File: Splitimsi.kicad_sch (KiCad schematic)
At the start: 44 parts, among them SW1 MX_RGB, SW10 MX_RGB, SW11 MX_RGB, SW12 RotaryEncoder_Switch, SW13 MX_RGB, SW14 MX_RGB, SW15 MX_RGB, SW16 MX_RGB, SW17 MX_RGB, SW18 MX_RGB, SW19 MX_RGB, SW2 MX_RGB, SW20 MX_RGB, SW21 MX_RGB, SW22 MX_RGB, SW23 MX_RGB, SW24 MX_RGB, SW25 MX_RGB, SW26 MX_RGB, SW27 MX_RGB, SW28 MX_RGB, SW29 MX_RGB, SW3 MX_RGB, SW30 MX_RGB, SW4 MX_RGB, SW5 MX_RGB, SW6 RotaryEncoder_Switch, SW7 MX_RGB, SW8 MX_RGB, SW9 MX_RGB, U1 ProMicro, U2 TRRS

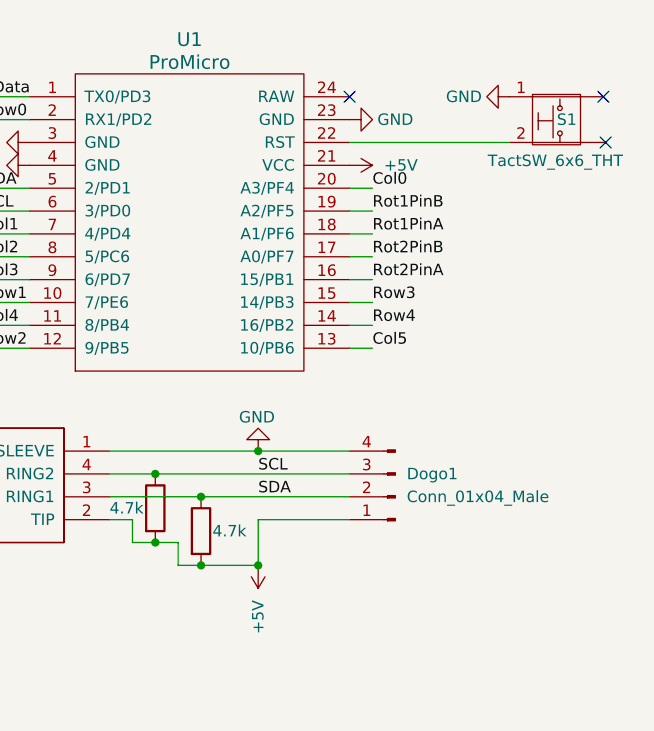
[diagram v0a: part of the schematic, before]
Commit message: reset schematic changed
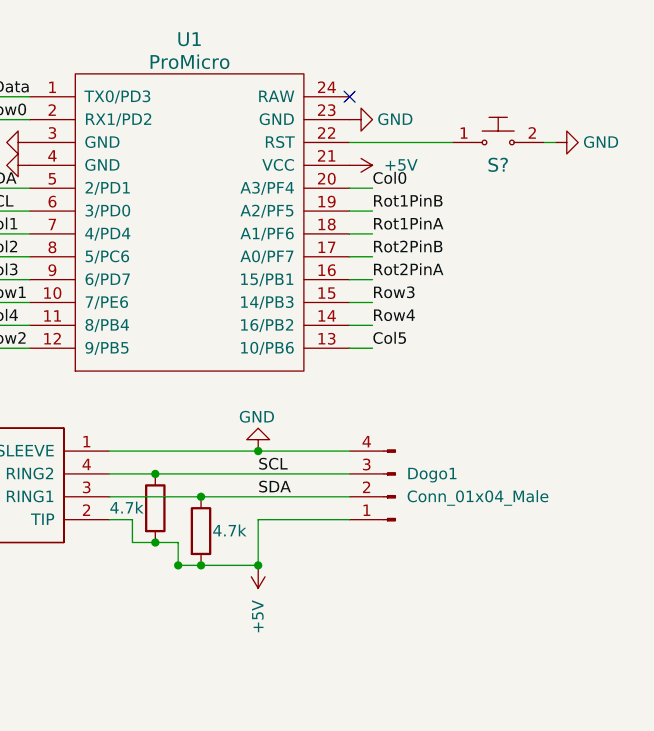
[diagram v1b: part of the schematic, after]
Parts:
- removed S1: TactSW_6x6_THT, Button_Switch_SMD:SW_SPST_B3U-1000P, symbol KeyboardCustomSym:TactSW_6x6_THT
- added S?: (no value), symbol dk_Tactile-Switches:B3U-1000P
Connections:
- net GND: now also S?.2
- net at U1.22 (RST): now also S?.1
- no-connect marks 3 -> 1
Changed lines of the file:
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@@
   (junction (at 63.5 101.6) (diameter 0) (color 0 0 0 0)
   )
+  (junction (at 170.18 73.66) (diameter 0) (color 0 0 0 0)
+  )
   (junction (at 73.66 71.12) (diameter 0) (color 0 0 0 0)
   )
@@
   )
   (no_connect (at 189.23 21.59))
-  (no_connect (at 217.424 21.59))
-  (no_connect (at 217.678 26.67))
+  (wire (pts (xy 210.82 26.67) (xy 212.09 26.67))
+    (stroke (width 0) (type default) (color 0 0 0 0))
+  )
   (wire (pts (xy 71.12 96.52) (xy 71.12 99.06))
     (stroke (width 0) (type default) (color 0 0 0 0))
@@
     (stroke (width 0) (type default) (color 0 0 0 0))
   )
-  (wire (pts (xy 189.23 26.67) (xy 207.01 26.67))
+  (wire (pts (xy 189.23 26.67) (xy 200.66 26.67))
     (stroke (width 0) (type default) (color 0 0 0 0))
   )
@@
   )
   (wire (pts (xy 97.79 128.27) (xy 104.14 128.27))
+    (stroke (width 0) (type default) (color 0 0 0 0))
+  )
+  (wire (pts (xy 170.18 73.7663) (xy 170.18 73.66))
     (stroke (width 0) (type default) (color 0 0 0 0))
   )
@@
     (pin "1")
   )
-  (symbol (lib_id "power:GND") (at 207.01 21.59 270) (unit 1)
-    (in_bom yes) (on_board yes)
-    (property "Reference" "#PWR01" (id 0) (at 200.66 21.59 0)
-      (effects (font (size 1.27 1.27)) hide)
-    )
-    (property "Value" "GND" (id 1) (at 201.93 21.59 90))
-    (property "Footprint" "" (id 2) (at 207.01 21.59 0)
-      (effects (font (size 1.27 1.27)) hide)
-    )
-    (property "Datasheet" "" (id 3) (at 207.01 21.59 0)
+  (symbol (lib_id "power:GND") (at 212.09 26.67 90) (unit 1)
+    (in_bom yes) (on_board yes)
+    (property "Reference" "#PWR01" (id 0) (at 218.44 26.67 0)
+      (effects (font (size 1.27 1.27)) hide)
+    )
+    (property "Value" "GND" (id 1) (at 217.17 26.67 90))
+    (property "Footprint" "" (id 2) (at 212.09 26.67 0)
+      (effects (font (size 1.27 1.27)) hide)
+    )
+    (property "Datasheet" "" (id 3) (at 212.09 26.67 0)
       (effects (font (size 1.27 1.27)) hide)
     )
@@
     (pin "8")
   )
+  (symbol (lib_id "dk_Tactile-Switches:B3U-1000P") (at 205.74 26.67 0) (unit 1)
+    (in_bom yes) (on_board yes)
+    (property "Reference" "S?" (id 0) (at 205.74 29.21 0)
+      (effects (font (size 1.524 1.524)))
+    )
+    (property "Value" "" (id 1) (at 205.74 21.59 0)
+      (effects (font (size 1.524 1.524)))
+    )
+    (property "Footprint" "" (id 2) (at 210.82 21.59 0)
+      (effects (font (size 1.524 1.524)) (justify left) hide)
+    )
+    (property "Datasheet" "https://omronfs.omron.com/en_US/ecb/products/pdf/en-b3u.pdf" (id 3) (at 210.82 19.05 0)
+      (effects (font (size 1.524 1.524)) (justify left) hide)
+    )
+    (property "Digi-Key_PN" "SW1020CT-ND" (id 4) (at 210.82 16.51 0)
+      (effects (font (size 1.524 1.524)) (justify left) hide)
+    )
+    (property "MPN" "B3U-1000P" (id 5) (at 210.82 13.97 0)
+      (effects (font (size 1.524 1.524)) (justify left) hide)
+    )
+    (property "Category" "Switches" (id 6) (at 210.82 11.43 0)
+      (effects (font (size 1.524 1.524)) (justify left) hide)
+    )
+    (property "Family" "Tactile Switches" (id 7) (at 210.82 8.89 0)
+      (effects (font (size 1.524 1.524)) (justify left) hide)
+    )
+    (property "DK_Datasheet_Link" "https://omronfs.omron.com/en_US/ecb/products/pdf/en-b3u.pdf" (id 8) (at 210.82 6.35 0)
+      (effects (font (size 1.524 1.524)) (justify left) hide)
+    )
+    (property "DK_Detail_Page" "/product-detail/en/omron-electronics-inc-emc-div/B3U-1000P/SW1020CT-ND/1534357" (id 9) (at 210.82 3.81 0)
+      (effects (font (size 1.524 1.524)) (justify left) hide)
+    )
+    (property "Description" "SWITCH TACTILE SPST-NO 0.05A 12V" (id 10) (at 210.82 1.27 0)
+      (effects (font (size 1.524 1.524)) (justify left) hide)
+    )
+    (property "Manufacturer" "Omron Electronics Inc-EMC Div" (id 11) (at 210.82 -1.27 0)
+      (effects (font (size 1.524 1.524)) (justify left) hide)
+    )
+    (property "Status" "Active" (id 12) (at 210.82 -3.81 0)
+      (effects (font (size 1.524 1.524)) (justify left) hide)
+    )
+    (pin "1")
+    (pin "2")
+  )
   (symbol (lib_id "power:GND") (at 82.55 109.22 0) (unit 1)
     (in_bom yes) (on_board yes)
@@
     )
     (pin "1")
-  )
-  (symbol (lib_id "KeyboardCustomSym:TactSW_6x6_THT") (at 213.106 24.13 0) (unit 1)
-    (in_bom yes) (on_board yes)
-    (property "Reference" "S1" (id 0) (at 213.36 24.13 0))
-    (property "Value" "TactSW_6x6_THT" (id 1) (at 212.09 28.702 0))
-    (property "Footprint" "Button_Switch_SMD:SW_SPST_B3U-1000P" (id 2) (at 212.09 20.066 0)
-      (effects (font (size 1.27 1.27)) hide)
-    )
-    (property "Datasheet" "" (id 3) (at 212.09 20.066 0)
-      (effects (font (size 1.27 1.27)) hide)
-    )
-    (pin "")
-    (pin "")
-    (pin "1")
-    (pin "2")
   )
   (symbol (lib_id "Keeb_SCH:TRRS") (at 153.67 58.42 180) (unit 1)
@@
       (reference "R2") (unit 1) (value "4.7k") (footprint "Resistor_SMD:R_1206_3216Metric_Pad1.30x1.75mm_HandSolder")
     )
-    (path "/a2474201-d835-4ea6-9d62-0592a109ce48"
-      (reference "S1") (unit 1) (value "TactSW_6x6_THT") (footprint "Button_Switch_SMD:SW_SPST_B3U-1000P")
+    (path "/71fa3c88-abdf-4868-92dd-da7a96a3466b"
+      (reference "S?") (unit 1) (value "B3U-1000P") (footprint "digikey-footprints:Switch_Tactile_SMD_B3U-1000P")
     )
     (path "/200aa83c-0260-4790-a345-ddeba1e13353"

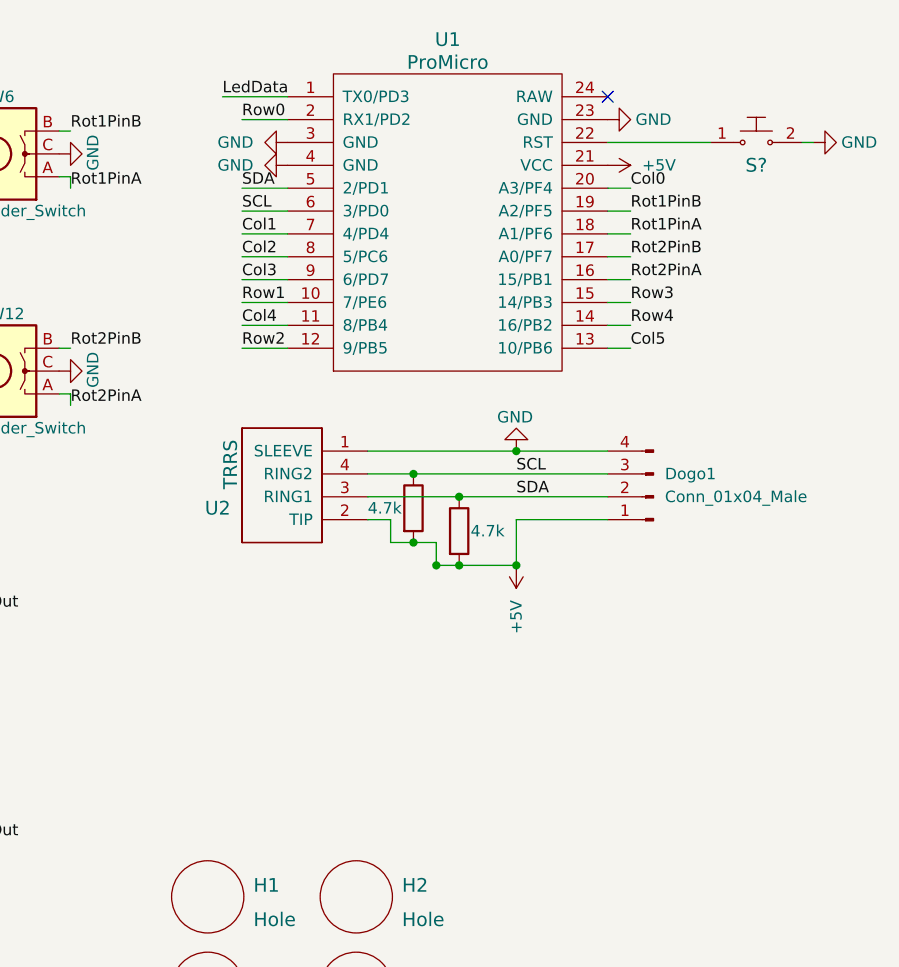
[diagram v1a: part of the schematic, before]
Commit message: slider switch added test
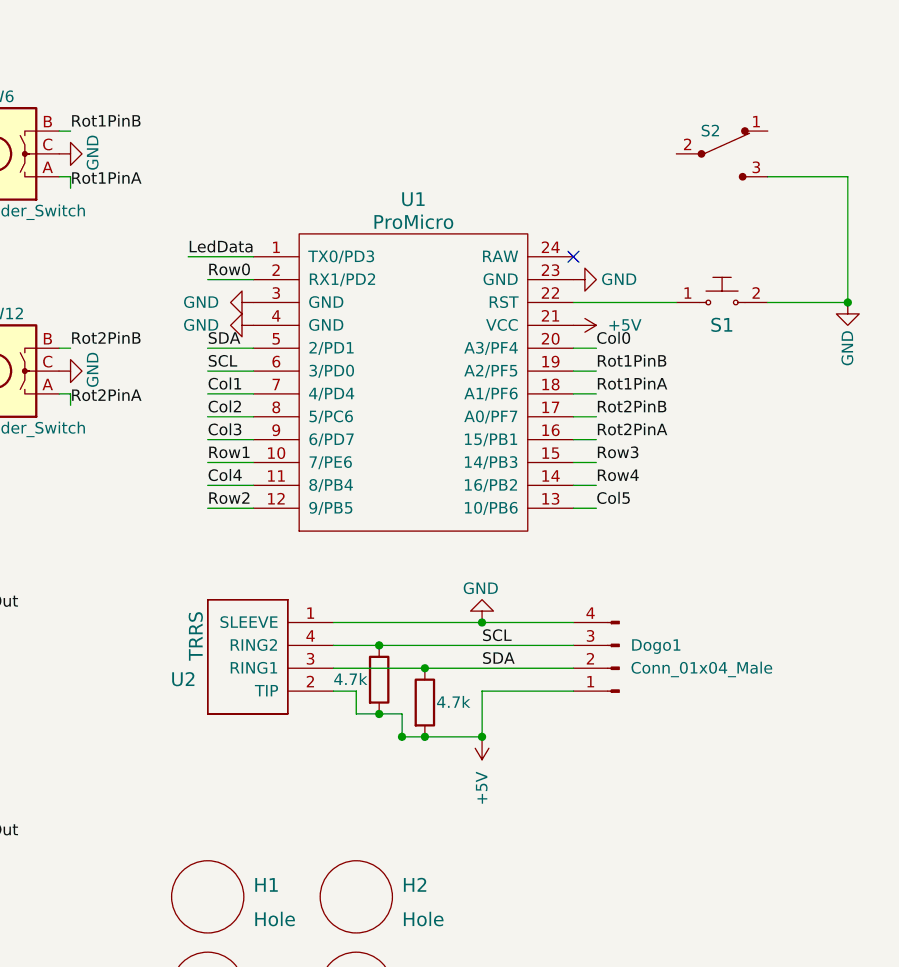
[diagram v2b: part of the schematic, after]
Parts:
- added S2: (no value), symbol dk_Slide-Switches:EG1218
- gave numbers to parts that had none: 1
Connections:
- net GND: now also S2.3
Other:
- moved on the sheet: Dogo1, S1, U1, U2

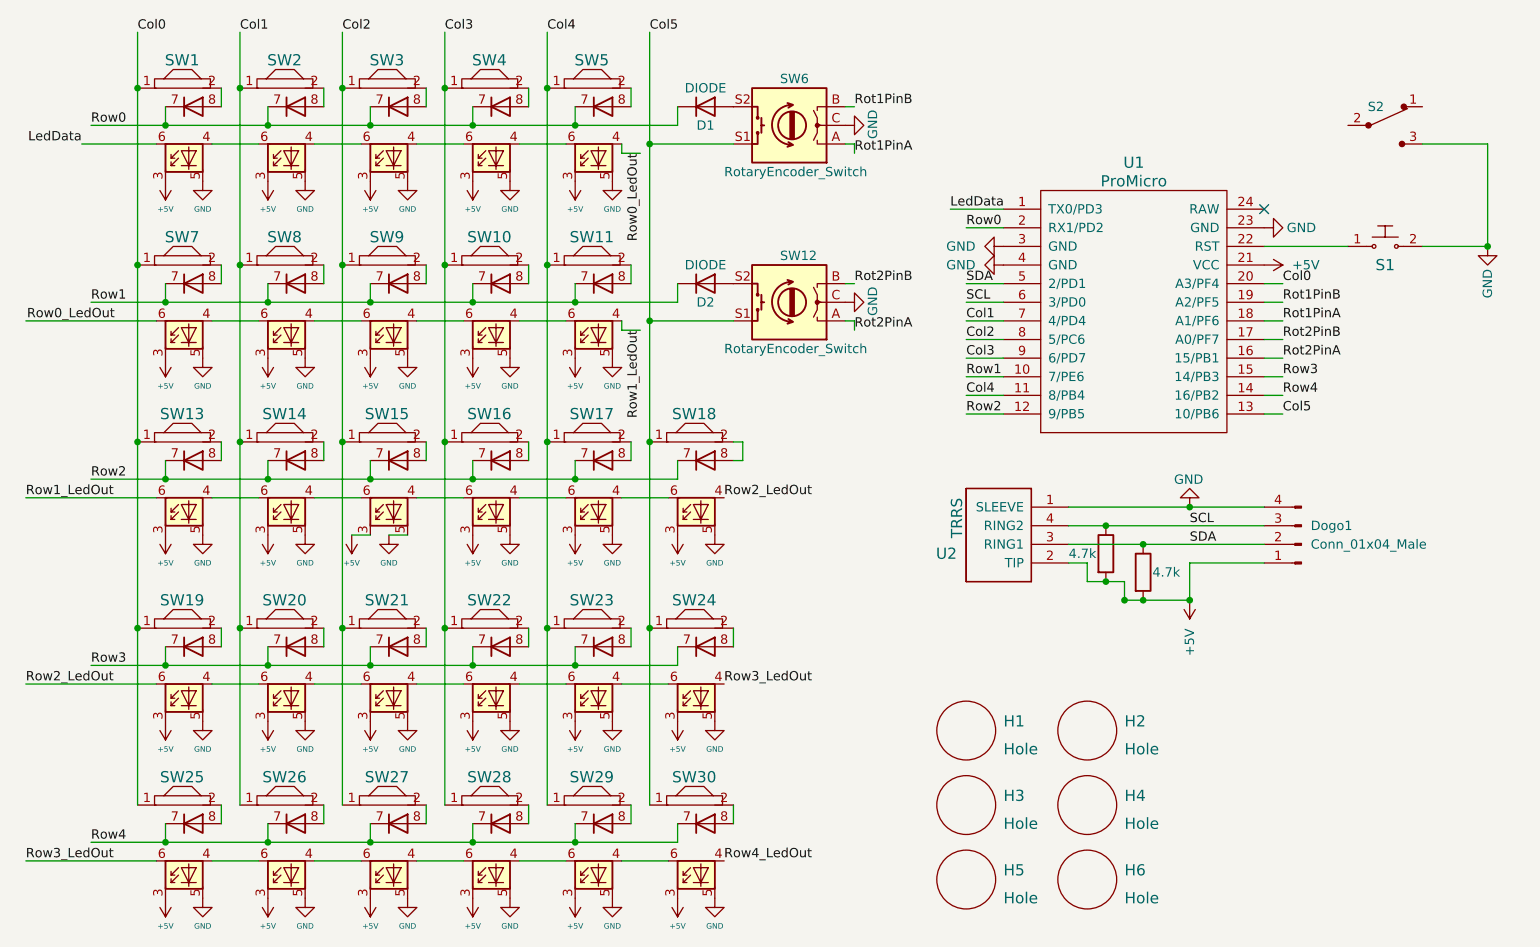
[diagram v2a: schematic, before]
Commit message: Power Flags added
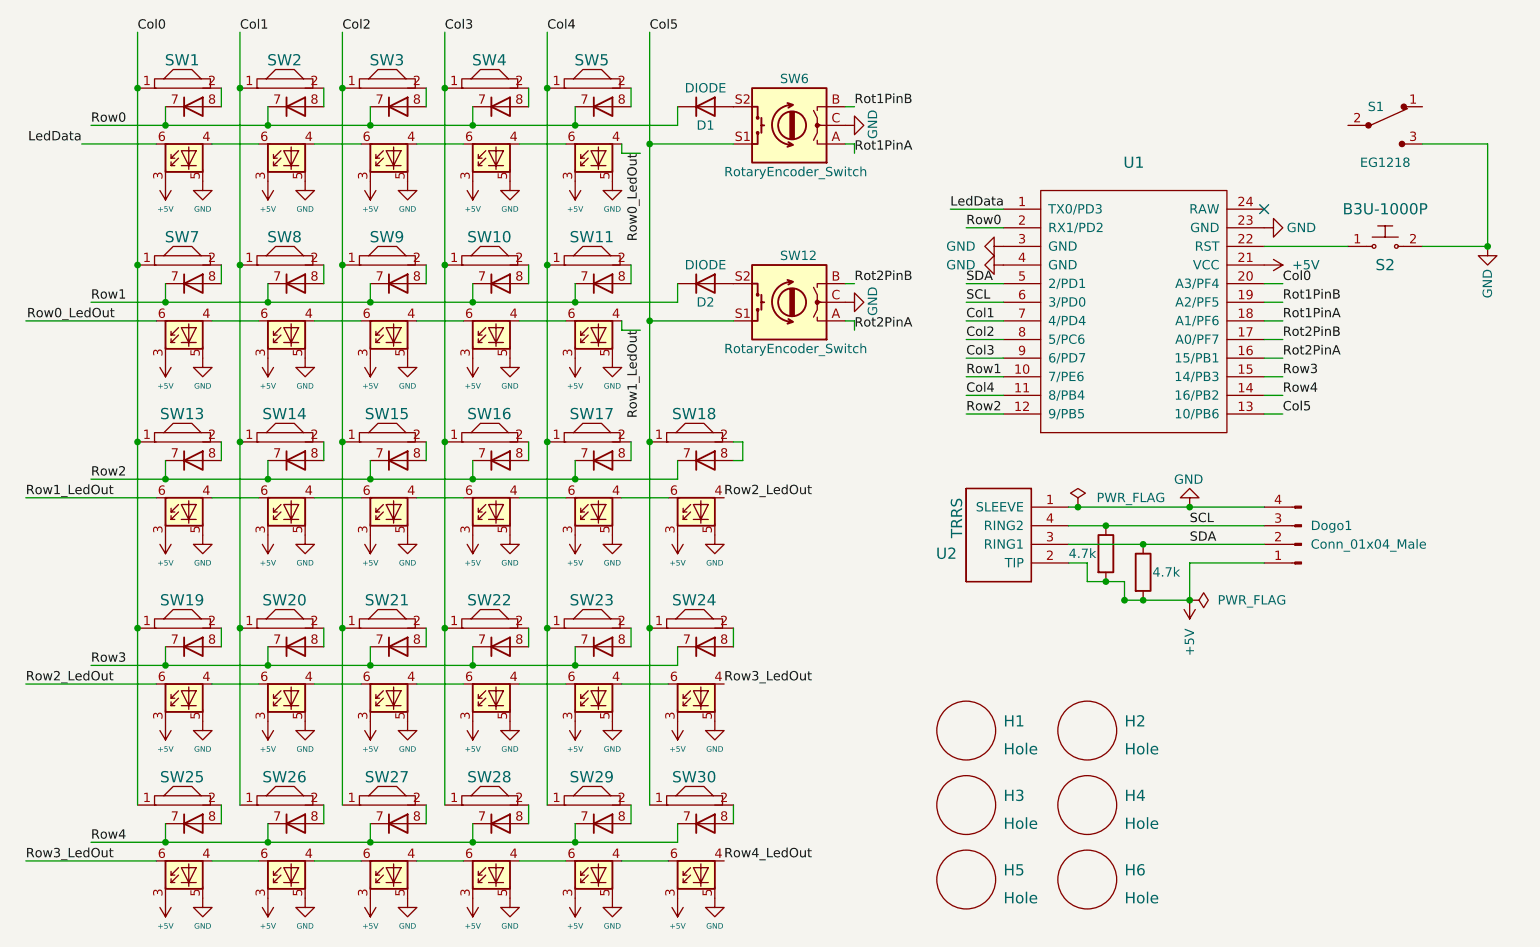
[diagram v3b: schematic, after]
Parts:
- S1: renamed from S2; value (none) -> EG1218; footprint (none) -> digikey-footprints:Switch_Slide_11.6x4mm_EG1218
- S2: renamed from S1; value (none) -> B3U-1000P; footprint (none) -> digikey-footprints:Switch_Tactile_SMD_B3U-1000P
- U1: value ProMicro -> (none); footprint Keebio-Parts:ArduinoProMicro -> (none)
